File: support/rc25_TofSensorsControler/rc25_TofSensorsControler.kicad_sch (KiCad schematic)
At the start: 13 parts, among them J1 Rear LPn, J2 Front LPn, J3 Rear I2C, J4 Front I2C, U1 RP2040-Zero, U3 VL53L8CX, U4 VL53L8CX, U5 VL53L8CX, U6 VL53L8CX, U7 VL53L8CX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

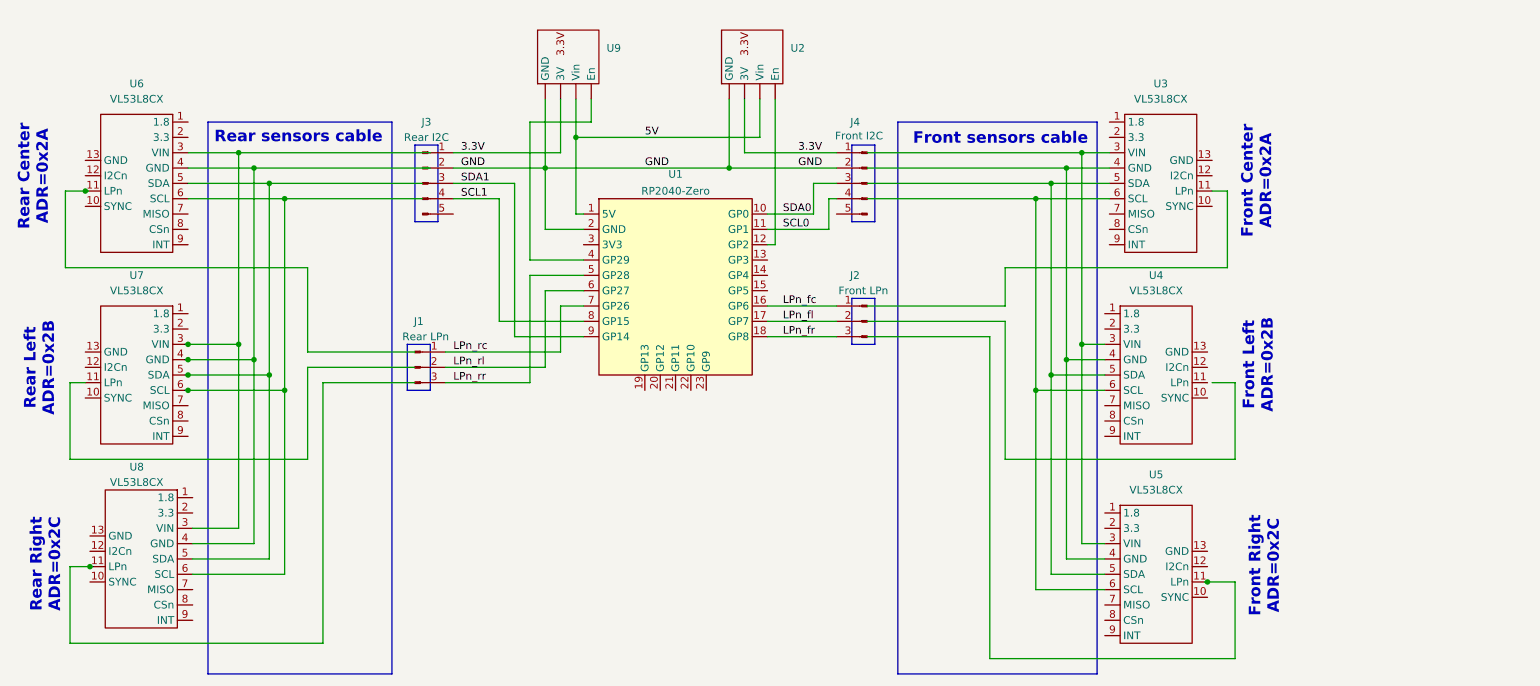
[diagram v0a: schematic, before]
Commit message: tof schematic: added I2C buffers
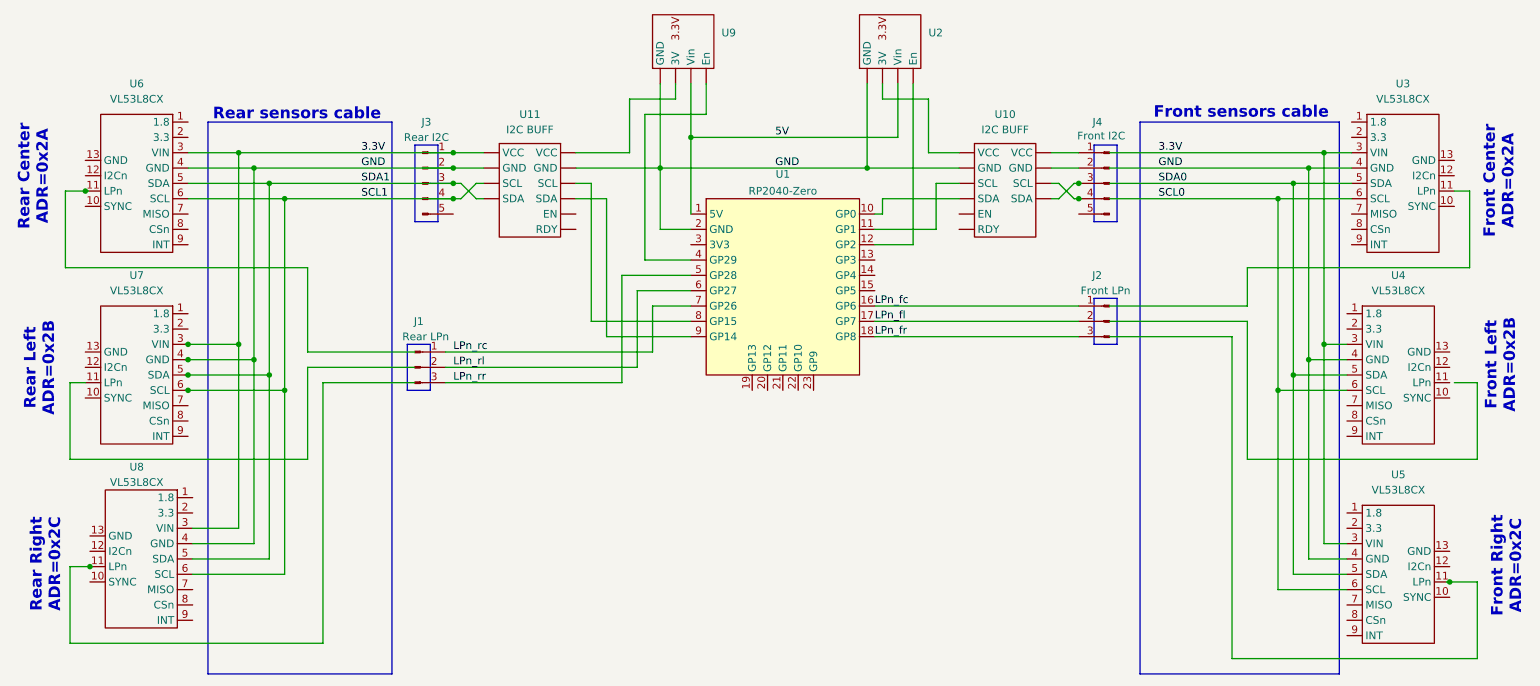
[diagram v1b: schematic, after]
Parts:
- added U10, U11: I2C BUFF, symbol MyRobot:Adafruit_I2C_Buffer
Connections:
- net 3.3V: now also U3.3 (VIN), U4.3 (VIN), U5.3 (VIN), U6.3 (VIN), U7.3 (VIN), U8.3 (VIN), U11. (SDA); no longer J4.1 (Pin_1), U2. (En), U9. (En)
- net GND: now also U3.4 (GND), U4.4 (GND), U5.4 (GND), U6.4 (GND), U7.4 (GND), U8.4 (GND), U10. (SDA), U11. (SDA); no longer J4.2 (Pin_2)
- net SCL0: now also U3.6 (SCL), U4.6 (SCL), U5.6 (SCL); no longer J4.4 (Pin_4), U1.11 (GP1)
- net SCL1: now also U6.6 (SCL), U7.6 (SCL), U8.6 (SCL), U11. (SDA); no longer U1.8 (GP15)
- net SDA0: now also U3.5 (SDA), U4.5 (SDA), U5.5 (SDA); no longer J4.3 (Pin_3), U1.10 (GP0)
- net SDA1: now also U6.5 (SDA), U7.5 (SDA), U8.5 (SDA), U11. (SDA); no longer U1.9 (GP14)
- new net: J4.1 (Pin_1), U10. (SDA)
- new net: J4.2 (Pin_2), U10. (SDA)
- new net: J4.3 (Pin_3), U10. (SDA)
- new net: J4.4 (Pin_4), U10. (SDA)
- new net: U1.10 (GP0), U10. (SDA)
- new net: U1.11 (GP1), U10. (SDA)
- new net: U1.8 (GP15), U11. (SDA)
- new net: U1.9 (GP14), U11. (SDA)
- new net: U11. (SDA), U9. (En)
- new net: U10. (SDA), U2. (En)
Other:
- moved on the sheet: J2, J4, U1, U2, U3, U4, U5, U9

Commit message: support: clean up a level of ImuGps hierarchy.  Updated TofSensors schematic. Srduino: updated Tof power enable pin number .gitignore: fixed path issues
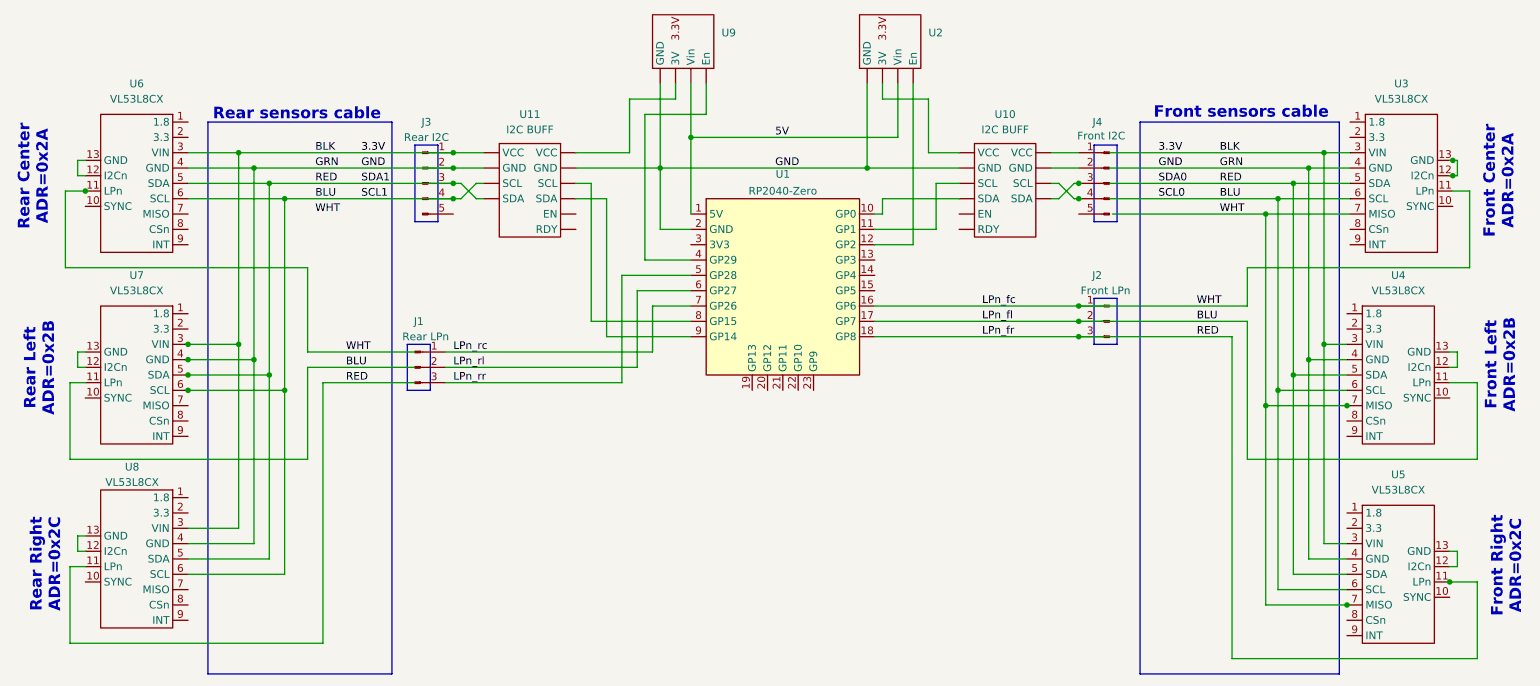
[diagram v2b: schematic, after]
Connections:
- net LPn_fl is gone; now on net BLU: J2.2 (Pin_2), U1.17 (GP7)
- net SCL0 is gone; now on net BLU: U3.6 (SCL), U4.6 (SCL), U5.6 (SCL)
- net SDA0 is gone; now on net LPn_fr: U3.5 (SDA), U4.5 (SDA), U5.5 (SDA)
- net SDA1 is gone; now on net LPn_fr: J3.3 (Pin_3), U11. (SDA), U6.5 (SDA), U7.5 (SDA), U8.5 (SDA)
- net LPn_fc: now also U3.11 (LPn), U3.7 (MISO), U4.7 (MISO), U5.7 (MISO), U6.11 (LPn)
- net LPn_fr: now also U5.11 (LPn), U8.11 (LPn)
- net BLU: now reaches U7.11 (LPn)
- net BLU: now also J3.4 (Pin_4), U11. (SDA), U4.11 (LPn), U6.6 (SCL), U7.6 (SCL), U8.6 (SCL)
- net at U7.12 (I2Cn): now also U7.13 (GND)
- net at U3.12 (I2Cn): now also U3.13 (GND)
- net at U5.12 (I2Cn): now also U5.13 (GND)
- net at U4.12 (I2Cn): now also U4.13 (GND)
- net at U6.12 (I2Cn): now also U6.13 (GND)
- net at U8.12 (I2Cn): now also U8.13 (GND)
- removed net SCL1: J3.4 (Pin_4), U11. (SDA), U6.6 (SCL), U7.6 (SCL), U8.6 (SCL)
- new net: U11. (SDA), U9. (En)
- new net: U10. (SDA), U2. (En)
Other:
- moved on the sheet: U8
